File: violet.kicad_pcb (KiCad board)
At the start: 2 copper layers, 13 parts, among them J1 NEIGHBOR1, J2 NEIGHBOR2, J7 BONUS_ROW, U1 M24C02-FMN6TP

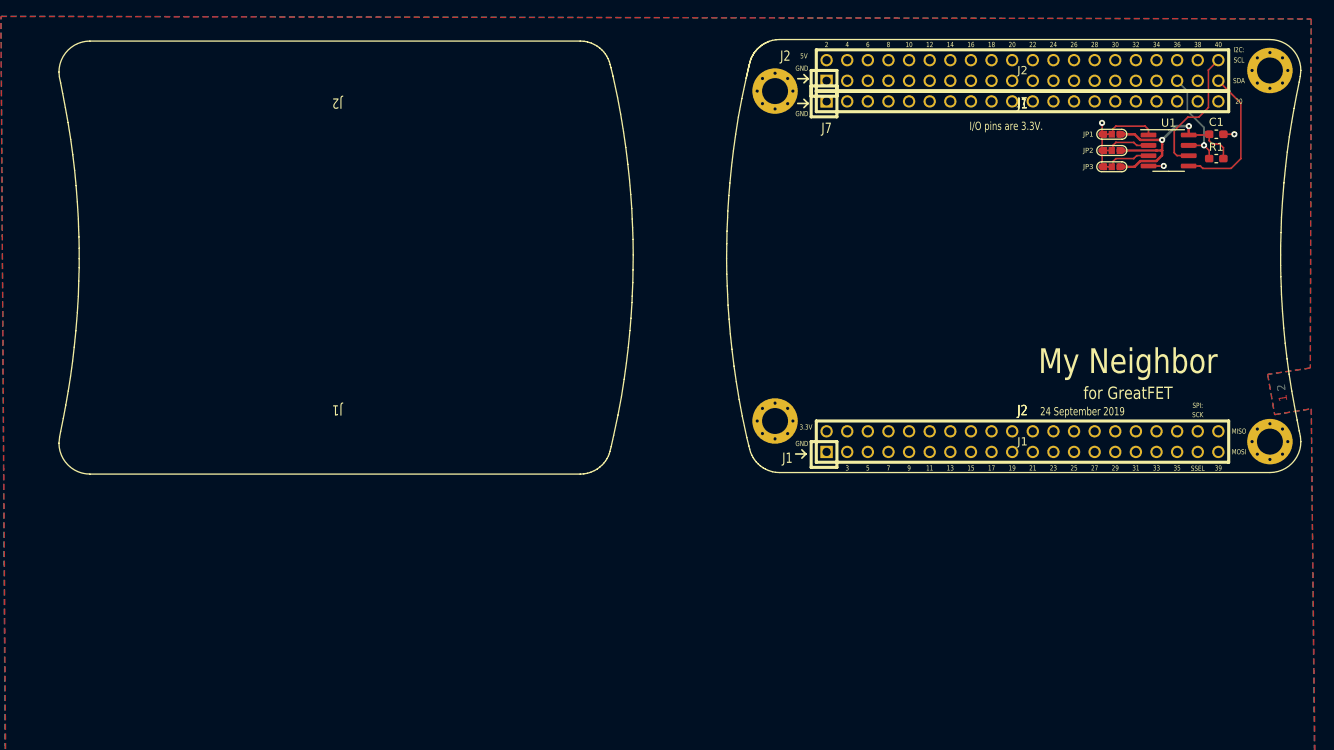
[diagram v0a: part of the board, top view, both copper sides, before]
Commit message: set up initial configuration of headers
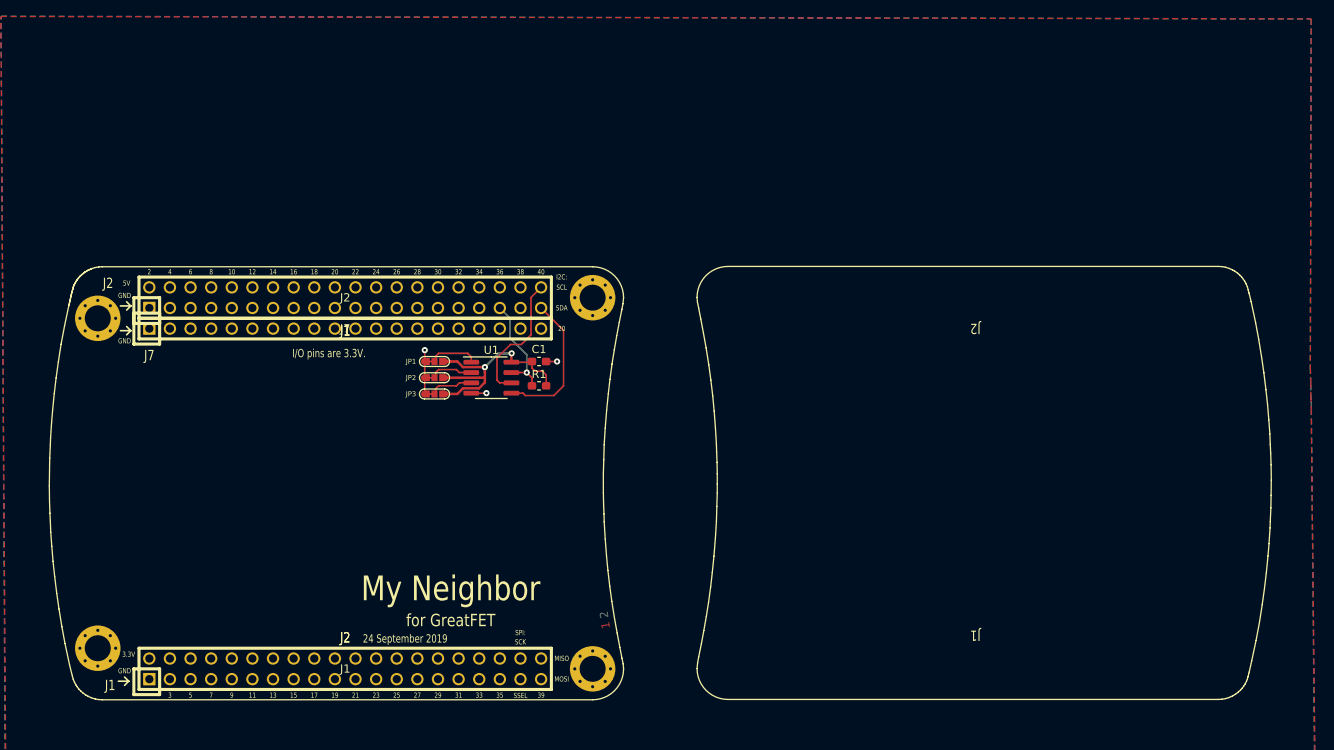
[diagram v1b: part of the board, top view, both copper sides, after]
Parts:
- moved MH1 88.0 mm to (40.3, 60.5)
- moved MH2 88.0 mm to (40.3, 101.1)
- moved MH3 88.0 mm to (101.3, 103.6)
- moved MH4 88.0 mm to (101.3, 57.9)
- moved C1 88.0 mm to (94.7, 65.8)
- moved J1 88.0 mm to (70.8, 103.6)
- moved J2 88.0 mm to (70.8, 57.9)
- moved J7 88.0 mm to (70.8, 61.7)
- moved JP1 88.0 mm to (81.8, 65.8)
- moved JP2 88.0 mm to (81.8, 67.8)
- moved JP3 88.0 mm to (81.8, 69.8)
- moved R1 88.0 mm to (94.7, 68.8)
- moved U1 88.0 mm to (88.8, 67.8)

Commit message: Place and orient headers on pcb
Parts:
- removed JP1, JP2, JP3: Jumper_3_Bridged12, neighbor:0603-JUMPER-3-BRIDGED12
- added C2: 100nF, gsg-modules:0603, F.Cu at (95.8, 5.87)
- added C3: 100nF, gsg-modules:0603, F.Cu at (105.9, -33.0)
- added C4: 100nF, gsg-modules:0603, F.Cu at (123.4, 3.45)
- added C5: 100nF, gsg-modules:0603, F.Cu at (119.5, 5.87)
- added C6: 100nF, gsg-modules:0603, F.Cu at (115.5, 5.87)
- added C7: 1uF, gsg-modules:0603, F.Cu at (111.6, 5.87)
- added C8: 1uF, gsg-modules:0603, F.Cu at (119.5, 3.45)
- added J10: Conn_01x08, gsg-modules:HEADER-1x8, F.Cu at (117.0, 69.2)
- added J3: NEIGHBOR1, gsg-modules:HEADER-2x20, B.Cu at (160.0, 91.6)
- added J4: BONUS_ROW, gsg-modules:HEADER-1x20, B.Cu at (160.0, 49.6)
- added J5: NEIGHBOR2, gsg-modules:HEADER-2x20, B.Cu at (160.0, 45.8)
- added J6: NEIGHBOR1, gsg-modules:HEADER-2x20, B.Cu at (191.4, 169.3)
- added J8: BONUS_ROW, gsg-modules:HEADER-1x20, B.Cu at (149.5, 169.2)
- added J9: NEIGHBOR2, gsg-modules:HEADER-2x20, B.Cu at (145.7, 169.2)
- added R10: 0.1, gsg-modules:0603, F.Cu at (115.5, 3.45)
- added R2: 12k, gsg-modules:0603, F.Cu at (103.7, 3.45)
- added R3: 12k, gsg-modules:0603, F.Cu at (99.8, 3.45)
- added R4: 12k, gsg-modules:0603, F.Cu at (95.8, 3.45)
- added R5: 12k, gsg-modules:0603, F.Cu at (107.7, 3.45)
- added R6: 12k, gsg-modules:0603, F.Cu at (99.8, 5.87)
- added R7: 12k, gsg-modules:0603, F.Cu at (103.7, 5.87)
- added R8: 12k, gsg-modules:0603, F.Cu at (107.7, 5.87)
- added R9: 43.2k, gsg-modules:0603, F.Cu at (111.6, 3.45)
- added U2: PCA9698, gsg-modules:TSSOP56, F.Cu at (99.0, -26.7)
- added U5: AP2553W6-7, gsg-modules:SOT457, F.Cu at (91.9, 4.34)
- C1: footprint Capacitor_SMD:C_0603_1608Metric_Pad1.05x0.95mm_HandSolder -> gsg-modules:0603
- J1, J2: footprint neighbor:HEADER-2x20 -> gsg-modules:HEADER-2x20; moved to B.Cu
- J7: footprint neighbor:HEADER-1x20 -> gsg-modules:HEADER-1x20; moved to B.Cu
- R1: value 10k -> 12k; footprint Resistor_SMD:R_0603_1608Metric_Pad1.05x0.95mm_HandSolder -> gsg-modules:0603
- U1: value M24C02-FMN6TP -> PCA9698; footprint Package_SO:SOIC-8_3.9x4.9mm_P1.27mm -> gsg-modules:TSSOP56
- moved C1 105.1 mm to (154.7, -20.5)
- moved R1 82.8 mm to (130.1, -6.02)
- moved U1 65.0 mm to (97.0, 132.2)
- moved J1 57.9 mm to (74.4, 45.9)
- moved J2 33.8 mm to (74.4, 91.6)
- moved J7 26.3 mm to (74.4, 87.8)
- moved MH3 12.6 mm to (104.9, 91.6)
- moved MH1 12.6 mm to (43.9, 48.4)
- moved MH4 12.6 mm to (104.9, 45.9)
- moved MH2 12.6 mm to (43.9, 89.0)
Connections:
- C1 pad 1: GND -> VCC
- C1 pad 2: VCC -> GND
- J7 pad 20: VCC -> Net-(J7-Pad20)
- R1 pad 1: /P2_1 -> VCC
- R1 pad 2: VCC -> /P9_6
- U1 pad 1: /E0 -> /I2C0_SDA
- U1 pad 2: /E1 -> /I2C0_SCL
- U1 pad 3: /E2 -> /U1_IO0_0
- U1 pad 4: GND -> /U1_IO0_1
- U1 pad 5: /I2C0_SDA -> Net-(U1-Pad5)
- U1 pad 6: /I2C0_SCL -> GND
- U1 pad 7: /P2_1 -> /U1_IO0_3
- U1 pad 8: VCC -> /U1_IO0_4
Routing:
- net VCC: track 29.9 -> 0.00 mm, vias 2 -> 0
- net /I2C0_SDA: track 17.8 -> 0.00 mm
- net /I2C0_SCL: track 16.4 -> 0.00 mm
- net /P2_1: track 13.1 -> 0.00 mm, vias 1 -> 0
- net GND: track 8.65 -> 0.00 mm, vias 3 -> 0
- net /E0: track 6.02 -> 0.00 mm
- net /E2: track 5.33 -> 0.00 mm
- net /E1: track 5.33 -> 0.00 mm
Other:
- board text added: "Violet"
- board text added: "testing unit for Gladiolus"
- board text removed: "24 September 2019"
- board text removed: "I/O pins are 3.3V."
- board text removed: "J2"
- board text removed: "J7"
- board text removed: "MISO"
- board text removed: "MOSI"
- board text removed: "My Neighbor"
- board text removed: "SCK"
- board text removed: "SPI:"
- board text removed: "for GreatFET"

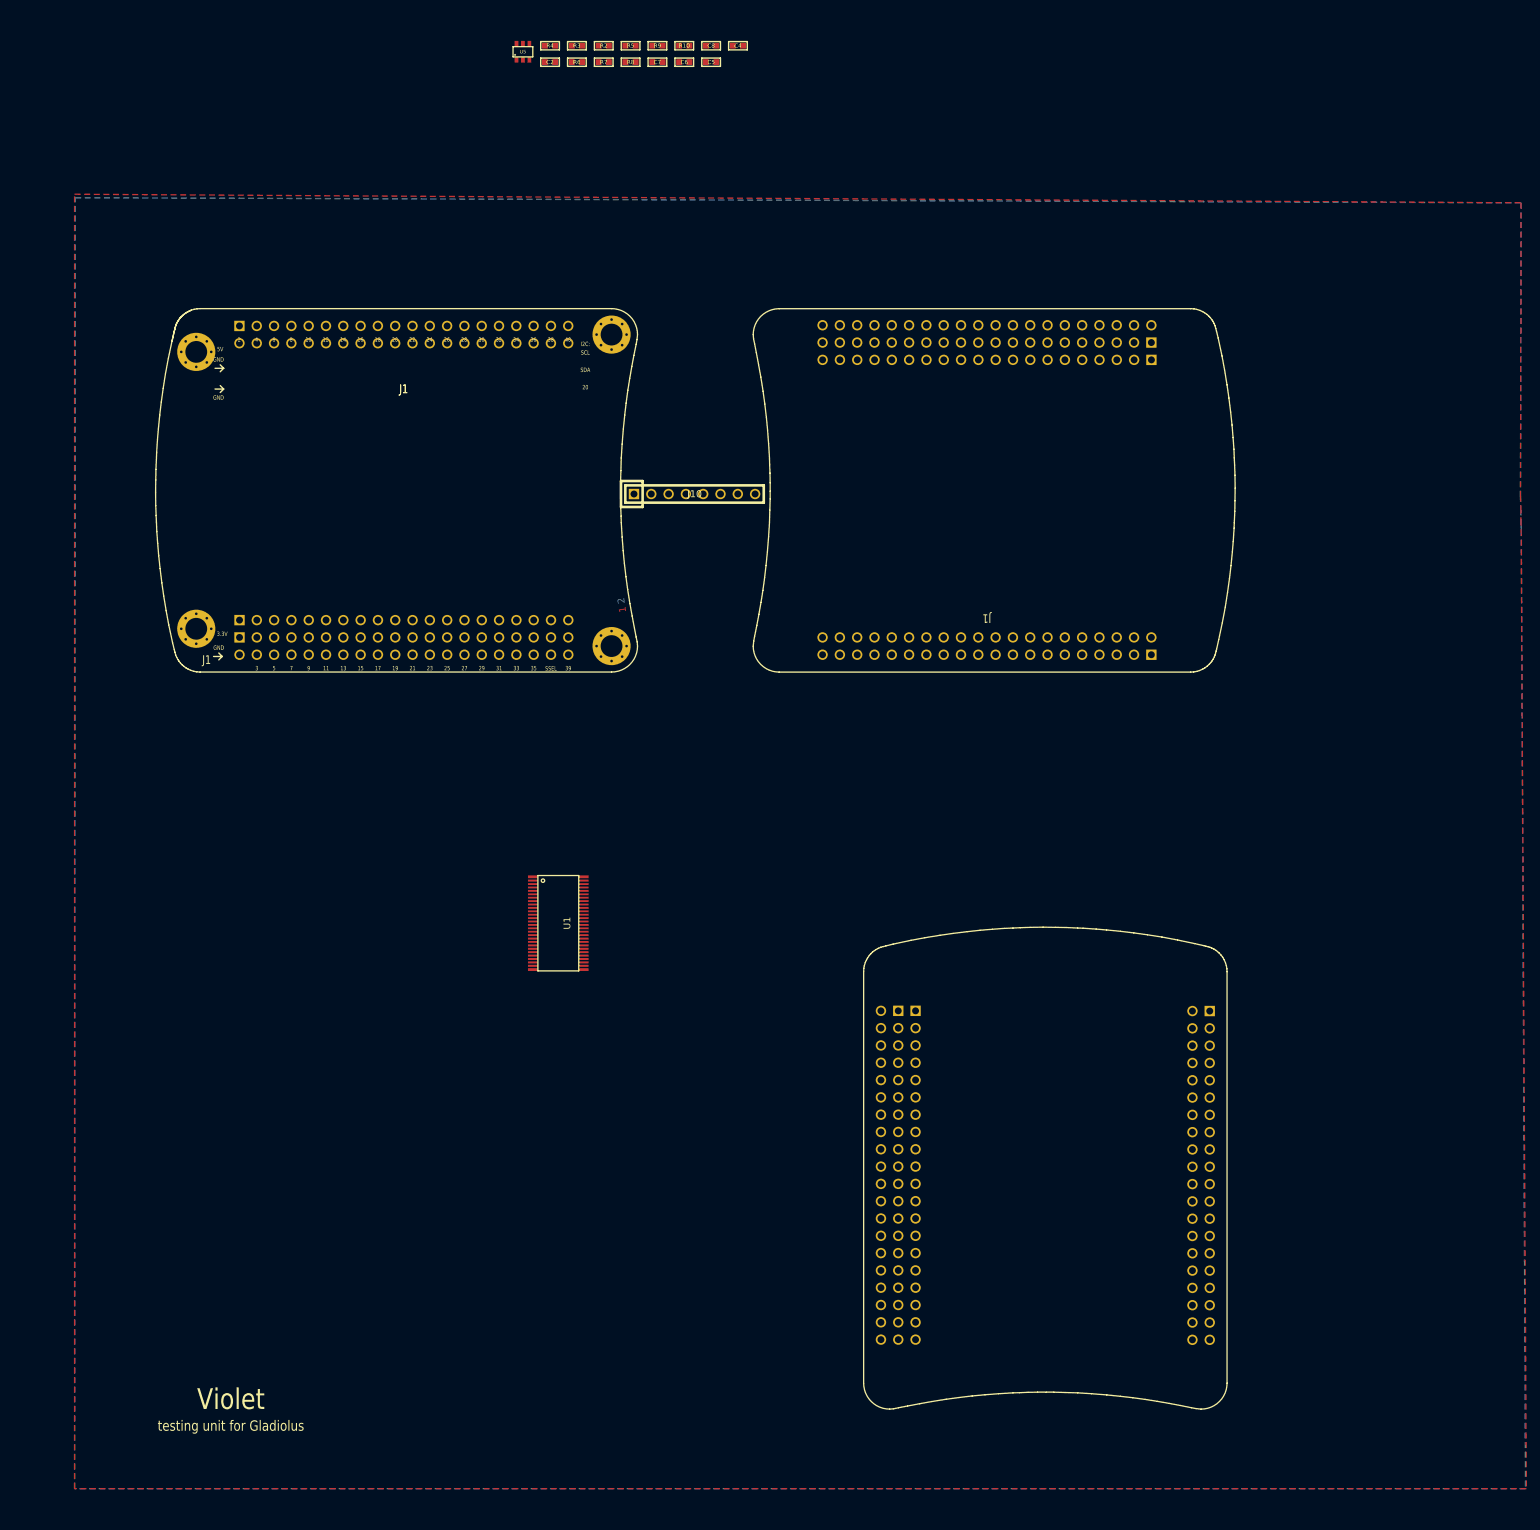
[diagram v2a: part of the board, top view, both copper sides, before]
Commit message: Layout power supply for EUT
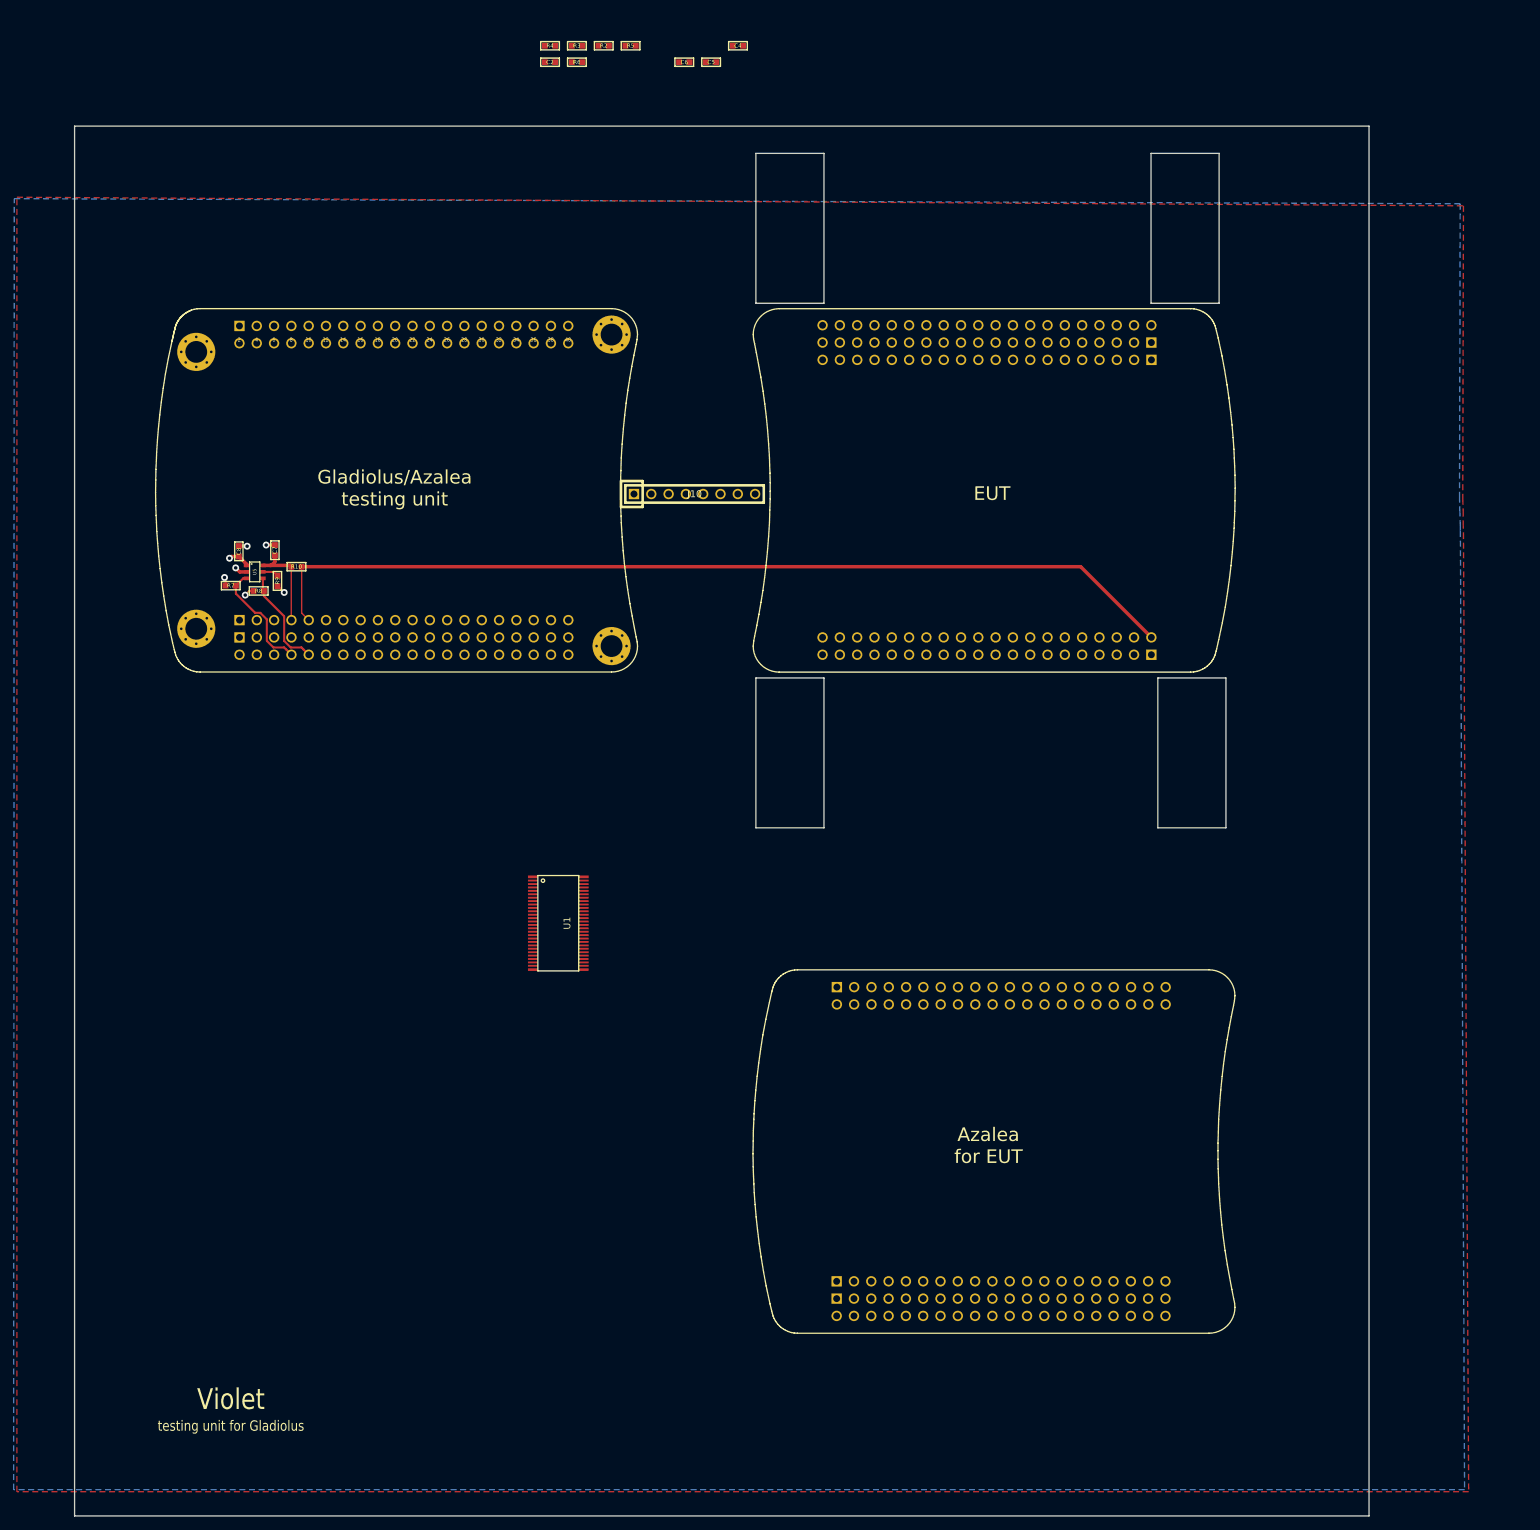
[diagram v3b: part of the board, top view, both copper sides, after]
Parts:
- moved C8 101.5 mm to (50.2, 77.7), turned to 90 degrees
- moved R9 96.3 mm to (55.8, 82.0), turned to 270 degrees
- moved R10 95.3 mm to (58.6, 79.9), turned to 180 degrees
- moved R8 94.9 mm to (53.1, 83.5)
- moved R7 94.3 mm to (49.0, 82.7), turned to 180 degrees
- moved C7 91.0 mm to (55.5, 77.5), turned to 90 degrees
- moved U5 85.9 mm to (52.5, 80.7), turned to 270 degrees
- moved J6 39.4 mm to (162.1, 142.9), turned to 0 degrees
- moved J9 25.4 mm to (162.0, 188.6), turned to 0 degrees
- moved J8 20.0 mm to (162.0, 184.8), turned to 0 degrees
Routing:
- net /ADC0_2: track 0.00 -> 137.3 mm
- net /P4_2: track 0.00 -> 16.9 mm
- net /P4_6: track 0.00 -> 14.9 mm
- net /ADC0_5: track 0.00 -> 14.0 mm
- net GND: track 0.00 -> 6.98 mm, vias 0 -> 5
- net VCC: track 0.00 -> 4.80 mm, vias 0 -> 2
- net Net-(R9-Pad1): track 0.00 -> 2.37 mm
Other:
- board outline added: 190 x 204 mm
- board text added: "Azalea for EUT"
- board text added: "EUT"
- board text added: "Gladiolus/Azalea testing unit"
- board text removed: "1"
- board text removed: "11"
- board text removed: "13"
- board text removed: "15"
- board text removed: "17"
- board text removed: "19"
- board text removed: "21"
- board text removed: "23"
- board text removed: "25"
- board text removed: "27"
- board text removed: "29"
- board text removed: "3"
- board text removed: "3.3V"
- board text removed: "31"
- board text removed: "33"
- board text removed: "35"
- board text removed: "39"
- board text removed: "5"
- board text removed: "5V"
- board text removed: "7"
- board text removed: "9"
- board text removed: "GND"
- board text removed: "I2C:"
- board text removed: "J1"
- board text removed: "SCL"
- board text removed: "SDA"
- board text removed: "SSEL"

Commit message: Wire J6 to J3
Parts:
- moved U2 152.9 mm to (99.0, 126.2), turned to 90 degrees
- moved U1 88.0 mm to (98.0, 44.2), turned to 90 degrees
- moved C7 16.1 mm to (57.5, 93.5)
- moved C8 16.1 mm to (52.2, 93.7)
- moved J1 16.1 mm to (76.4, 61.9)
- moved J10 16.1 mm to (119.0, 85.2)
- moved J2 16.1 mm to (76.4, 107.6)
- moved J3 16.1 mm to (162.0, 107.6)
- moved J4 16.1 mm to (162.0, 65.6)
- moved J5 16.1 mm to (162.0, 61.8)
- moved J7 16.1 mm to (76.4, 103.8)
- moved MH1 16.1 mm to (45.9, 64.4)
- moved MH2 16.1 mm to (45.9, 105.0)
- moved MH3 16.1 mm to (106.9, 107.6)
- moved MH4 16.1 mm to (106.9, 61.9)
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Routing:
- net /EUT_P1_16: track 0.00 -> 119.4 mm
- net /EUT_P1_15: track 0.00 -> 117.0 mm
- net /EUT_P5_6: track 0.00 -> 115.6 mm
- net /EUT_P1_13: track 0.00 -> 113.7 mm
- net /EUT_P1_14: track 0.00 -> 112.2 mm
- net /EUT_P5_4: track 0.00 -> 111.2 mm
- net /EUT_P5_5: track 0.00 -> 109.8 mm
- net /EUT_P1_11: track 0.00 -> 108.6 mm
- net /EUT_P1_12: track 0.00 -> 107.4 mm
- net /EUT_P1_10: track 0.00 -> 106.3 mm
- net /EUT_P5_3: track 0.00 -> 105.0 mm
- net /EUT_P1_8: track 0.00 -> 103.1 mm
- net /EUT_P1_9: track 0.00 -> 101.0 mm
- net /EUT_P1_6: track 0.00 -> 98.6 mm
- net /EUT_P1_7: track 0.00 -> 97.3 mm
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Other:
- outline, holes or cut-outs redrawn

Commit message: Wire J8/9 to J4/5; place new mounting holes; begin wiring U1
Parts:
- added MH10: MOUNTING_HOLE, gsg-modules:HOLE126MIL-COPPER, F.Cu at (31.1, 214.2)
- added MH11: MOUNTING_HOLE, gsg-modules:HOLE126MIL-COPPER, F.Cu at (143.1, 115.2)
- added MH12: MOUNTING_HOLE, gsg-modules:HOLE126MIL-COPPER, F.Cu at (182.1, 115.2)
- added MH13: MOUNTING_HOLE, gsg-modules:HOLE126MIL-COPPER, F.Cu at (162.1, 189.2)
- added MH14: MOUNTING_HOLE, gsg-modules:HOLE126MIL-COPPER, F.Cu at (162.1, 144.2)
- added MH15: MOUNTING_HOLE, gsg-modules:HOLE126MIL-COPPER, F.Cu at (77.0, 144.2)
- added MH16: MOUNTING_HOLE, gsg-modules:HOLE126MIL-COPPER, F.Cu at (77.0, 189.2)
- added MH5: MOUNTING_HOLE, gsg-modules:HOLE126MIL-COPPER, F.Cu at (31.1, 20.2)
- added MH6: MOUNTING_HOLE, gsg-modules:HOLE126MIL-COPPER, F.Cu at (211.1, 214.2)
- added MH7: MOUNTING_HOLE, gsg-modules:HOLE126MIL-COPPER, F.Cu at (143.1, 54.2)
- added MH8: MOUNTING_HOLE, gsg-modules:HOLE126MIL-COPPER, F.Cu at (211.1, 20.2)
- added MH9: MOUNTING_HOLE, gsg-modules:HOLE126MIL-COPPER, F.Cu at (181.1, 54.2)
- moved C3 180.1 mm to (102.8, 147.1), turned to 180 degrees
- moved C1 162.6 mm to (110.8, 136.1), turned to 90 degrees
- moved C2 145.4 mm to (114.2, 150.2), turned to 270 degrees
- moved U1 100.0 mm to (112.5, 143.2), turned to 270 degrees
- moved U2 88.6 mm to (103.0, 37.8)
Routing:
- net /EUT_P4_2: track 0.00 -> 208.8 mm
- net /EUT_P2_5: track 0.00 -> 208.0 mm
- net /EUT_ADC0_5: track 0.00 -> 206.5 mm
- net /EUT_P2_3: track 0.00 -> 206.4 mm
- net /EUT_P7_0: track 0.00 -> 205.9 mm
- net /EUT_ADC0_2: track 0.00 -> 205.5 mm
- net /EUT_P6_8: track 0.00 -> 204.9 mm
- net /EUT_P6_6: track 0.00 -> 201.7 mm
- net /EUT_P2_2: track 0.00 -> 201.1 mm
- net /EUT_P6_3: track 0.00 -> 199.9 mm
- net /EUT_I2C0_SCL: track 0.00 -> 195.8 mm
- net /EUT_I2C0_SDA: track 0.00 -> 192.5 mm
- net /U1_IO0_5: track 0.00 -> 61.8 mm
- net /I2C0_SCL: track 0.00 -> 60.5 mm, vias 0 -> 2
- net /U1_IO0_4: track 0.00 -> 57.2 mm
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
